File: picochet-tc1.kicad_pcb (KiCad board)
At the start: 4 copper layers, 58.7 x 27.8 mm, 53 parts, among them J1 Conn_01x02, J2 Conn_01x02, J3 Conn_01x04, J4 Conn_01x02, J5 Conn_02x02, J6 Conn_01x05, J7 Conn_01x03, Q1 DMT12H060LFDF, Q2 DMT12H060LFDF, SW1 SW_Push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

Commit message: Add QR link to repo, cleanup
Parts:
- added QR*****: github.com/eatnooM/picochet-tc1, rp2354_openfire:picochet-tc1-repo-qr, B.Cu at (157.7, 93.2)
- moved REF** 12.5 mm to (159.2, 79.7)
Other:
- board text added: "For use with OpenFIRE firmware: openfirelightgun.org"
- board text added: "Picochet-TC1 v0.1"
- board text removed: "v0.1 prototype - it might work"

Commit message: Small tweaks for v0.1 prototype
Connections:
- net /VREG_AVDD renamed VREG_AVDD

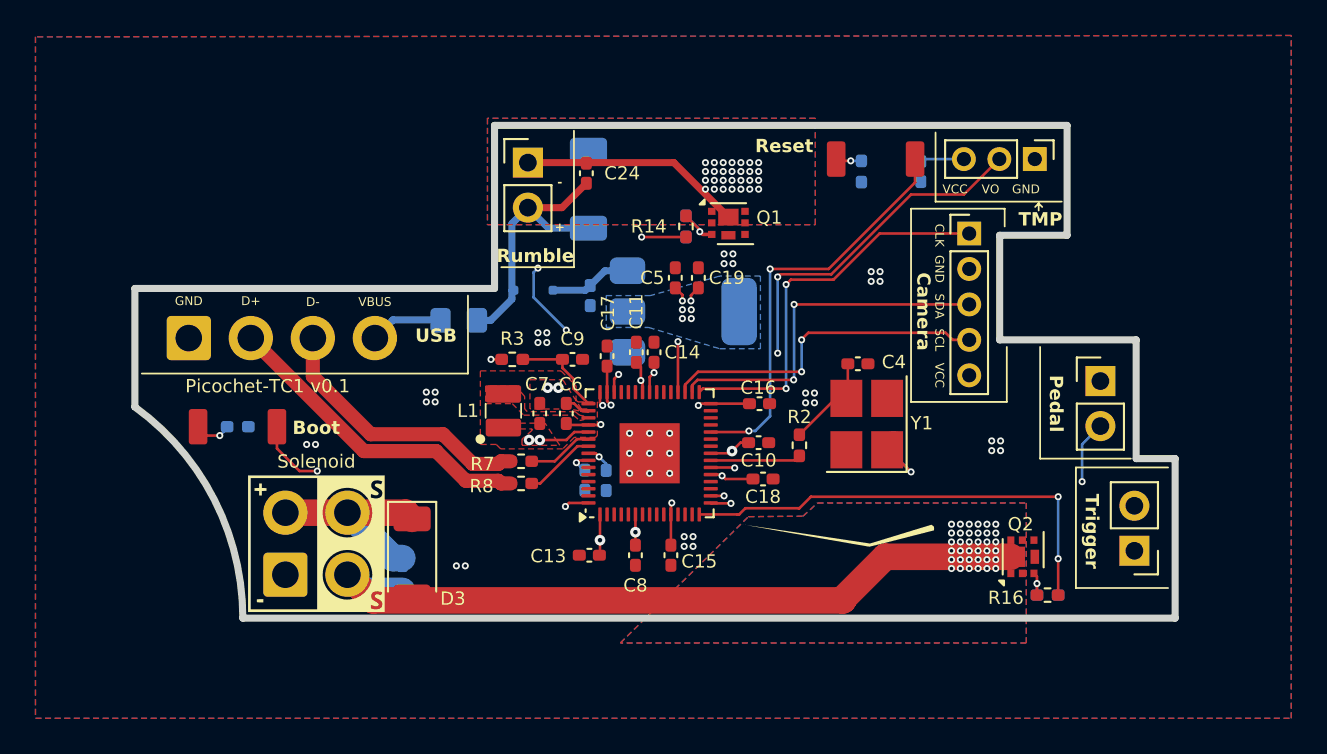
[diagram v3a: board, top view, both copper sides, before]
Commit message: Larger vias to keep JLC happy
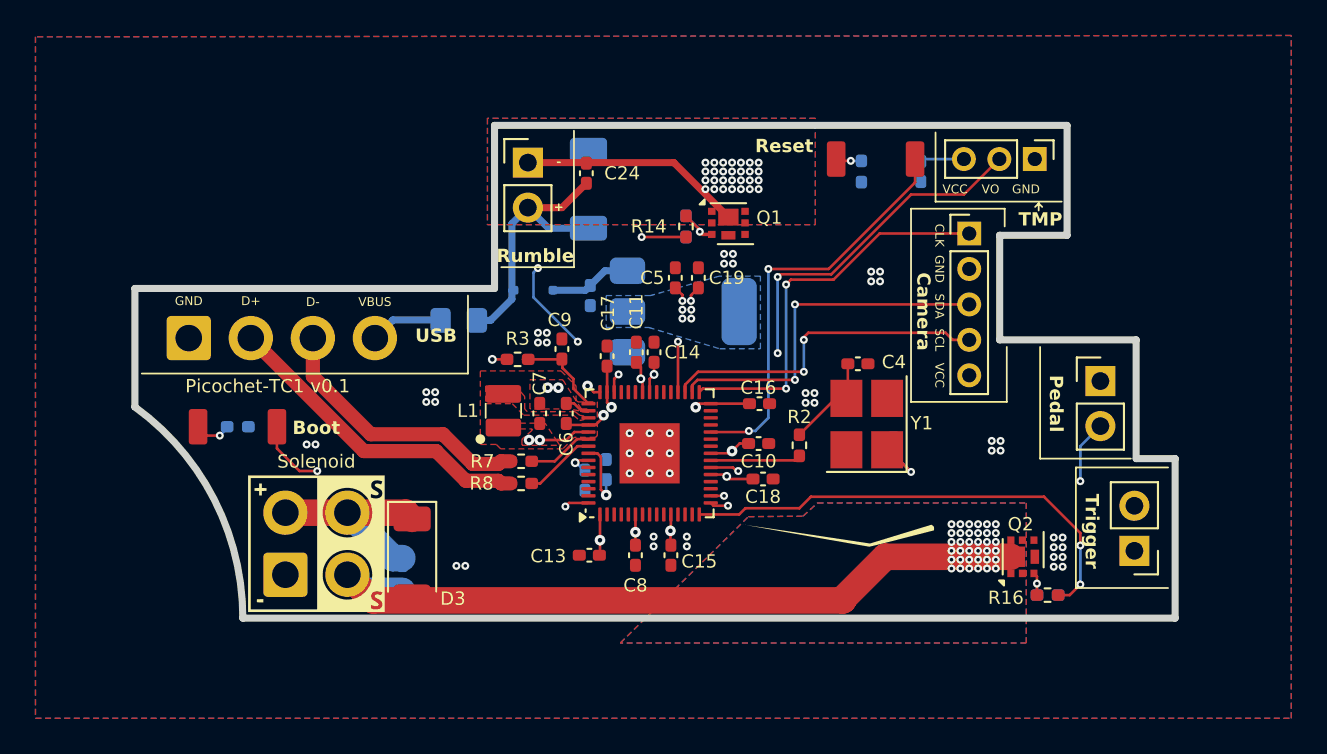
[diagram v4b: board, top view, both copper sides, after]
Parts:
- moved C9 0.84 mm to (143.8, 84.6), turned to -90 degrees
- moved C12 0.61 mm to (146.3, 91.4), turned to -90 degrees
- moved R3 0.30 mm to (141.3, 85.2)
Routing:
- net +3V3: track 24.9 -> 27.2 mm
- net /SOLENOID: track 26.1 -> 27.2 mm
- net Net-(C4-Pad2): track 5.64 -> 4.77 mm
- net Net-(U1-XIN): track 15.3 -> 14.5 mm
- net GND: vias 43 -> 51

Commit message: swap 10uF caps to 0805; tweak routing
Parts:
- C1, C19, C5: footprint Capacitor_SMD:C_0402_1005Metric_Pad0.74x0.62mm_HandSolder -> Capacitor_SMD:C_0805_2012Metric_Pad1.18x1.45mm_HandSolder
- moved C19 2.27 mm to (152.8, 82.5), turned to -90 degrees
- moved C5 2.19 mm to (148.2, 81.5), turned to 180 degrees
- moved C1 0.88 mm to (145.1, 80.8)
- moved C17 0.22 mm to (146.3, 84.8)
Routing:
- net +3V3: track 27.2 -> 29.0 mm
- net /RUMBLE: track 22.9 -> 21.1 mm, vias 4 -> 3

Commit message: Add options for second pedal and A/B buttons
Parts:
- removed R3: 33R, Resistor_SMD:R_0402_1005Metric_Pad0.72x0.64mm_HandSolder
- removed SW6: SW_Push, scorpion2:Switch-Push-SMD-4mmx3mm
- added C21: 10uF, Capacitor_SMD:C_0805_2012Metric_Pad1.18x1.45mm_HandSolder, B.Cu at (138.7, 83.8)
- added J8: Conn_01x03, Connector_PinHeader_2.54mm:PinHeader_1x03_P2.54mm_Vertical, F.Cu at (125.2, 89.8)
- added J9: Conn_01x02, Connector_PinHeader_2.54mm:PinHeader_1x02_P2.54mm_Vertical, F.Cu at (174.0, 89.8)
- added R5: 33R, Resistor_SMD:R_0402_1005Metric_Pad0.72x0.64mm_HandSolder, F.Cu at (141.3, 85.2)
- added SW2: SW_Push, scorpion2:Switch-Push-SMD-4mmx3mm, F.Cu at (161.5, 73.9)
- C24, C25: footprint Capacitor_SMD:C_0402_1005Metric_Pad0.74x0.62mm_HandSolder -> Capacitor_SMD:C_0805_2012Metric_Pad1.18x1.45mm_HandSolder
- C3: moved to F.Cu
- moved SW1 30.8 mm to (140.1, 96.1)
- moved R6 16.2 mm to (140.1, 96.1)
- moved C3 1.81 mm to (164.3, 90.4)
- moved F1 1.62 mm to (136.6, 83.8), turned to 90 degrees
- moved D1 1.50 mm to (142.2, 79.8)
- moved R7 1.25 mm to (141.5, 92.2)
- moved R8 1.25 mm to (141.5, 91.0)
- moved C24 0.50 mm to (145.4, 75.2)
- moved J4 0.25 mm to (174.1, 86.2), turned to -90 degrees
- moved C25 0.10 mm to (134.8, 97.3)
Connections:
- net /~{BTN_PEDAL} renamed /~{BTN_A}
- R7 pad 1: /USB_D- -> /USB_D+
- R7 pad 2: Net-(U1-USB_DM) -> Net-(U1-USB_DP)
- R8 pad 1: /USB_D+ -> /USB_D-
- R8 pad 2: Net-(U1-USB_DP) -> Net-(U1-USB_DM)
- SW1 pad 1: Net-(R4-Pad2) -> Net-(R6-Pad2)
- SW1 pad 2: /~{RESET} -> Net-(U1-~{QSPI_SS})
- U1 pad 18: unconnected-(U1-GPIO14-Pad18) -> /~{BTN_B}
- U1 pad 2: unconnected-(U1-GPIO0-Pad2) -> /~{BTN_PEDAL_1}
- U1 pad 3: unconnected-(U1-GPIO1-Pad3) -> /~{BTN_PEDAL_2}
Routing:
- net /~{BTN_PEDAL_1}: track 0.00 -> 24.8 mm, vias 0 -> 1
- net /~{BTN_PEDAL_2}: track 0.00 -> 22.3 mm, vias 0 -> 1
- net /~{BTN_B}: track 0.00 -> 21.5 mm, vias 0 -> 1
- net Net-(U1-~{QSPI_SS}): track 20.2 -> 5.20 mm
- net /USB_D-: track 15.4 -> 18.2 mm
- net /~{BTN_A}: track 24.8 -> 27.1 mm
- net +5V: track 15.8 -> 17.6 mm
- net Net-(R6-Pad2): track 2.02 -> 2.56 mm
- net GND: vias 51 -> 53
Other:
- board text added: "1"
- board text added: "2"
- board text added: "A"
- board text added: "B"
- board text added: "Picochet-TC1 v0.2"
- board text added: "Rumb"
- board text removed: "Picochet-TC1 v0.1"
